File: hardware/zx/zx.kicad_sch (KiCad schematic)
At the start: 51 parts, among them J1 ZX Keyboard, J10 Conn_01x01, J11 Conn_01x01, J12 Conn_01x01, J13 Conn_01x01, J14 Conn_01x01, J15 Conn_01x01, J16 Conn_01x01, J17 Conn_01x01, J18 Conn_01x01, J19 Conn_01x01, J2 GOTEK, J20 Conn_01x01, J21 Conn_01x01, J22 Conn_01x01, J23 Conn_01x01, J24 Conn_01x01, J25 Conn_01x01, J26 Conn_01x01, J27 Conn_01x01, J28 Conn_01x01, J29 Conn_01x01, J3 UART, J30 Conn_01x01, J4 USB_A, J5 USB_A, J6 Keyboard, J7 Mouse, J8 Kempston Mouse, J9 Z80, SW1 RESET, SW2 BOOT0, SW3 BOOT1, U1 CH559L, U2 CH446Q, Y1 12MHz

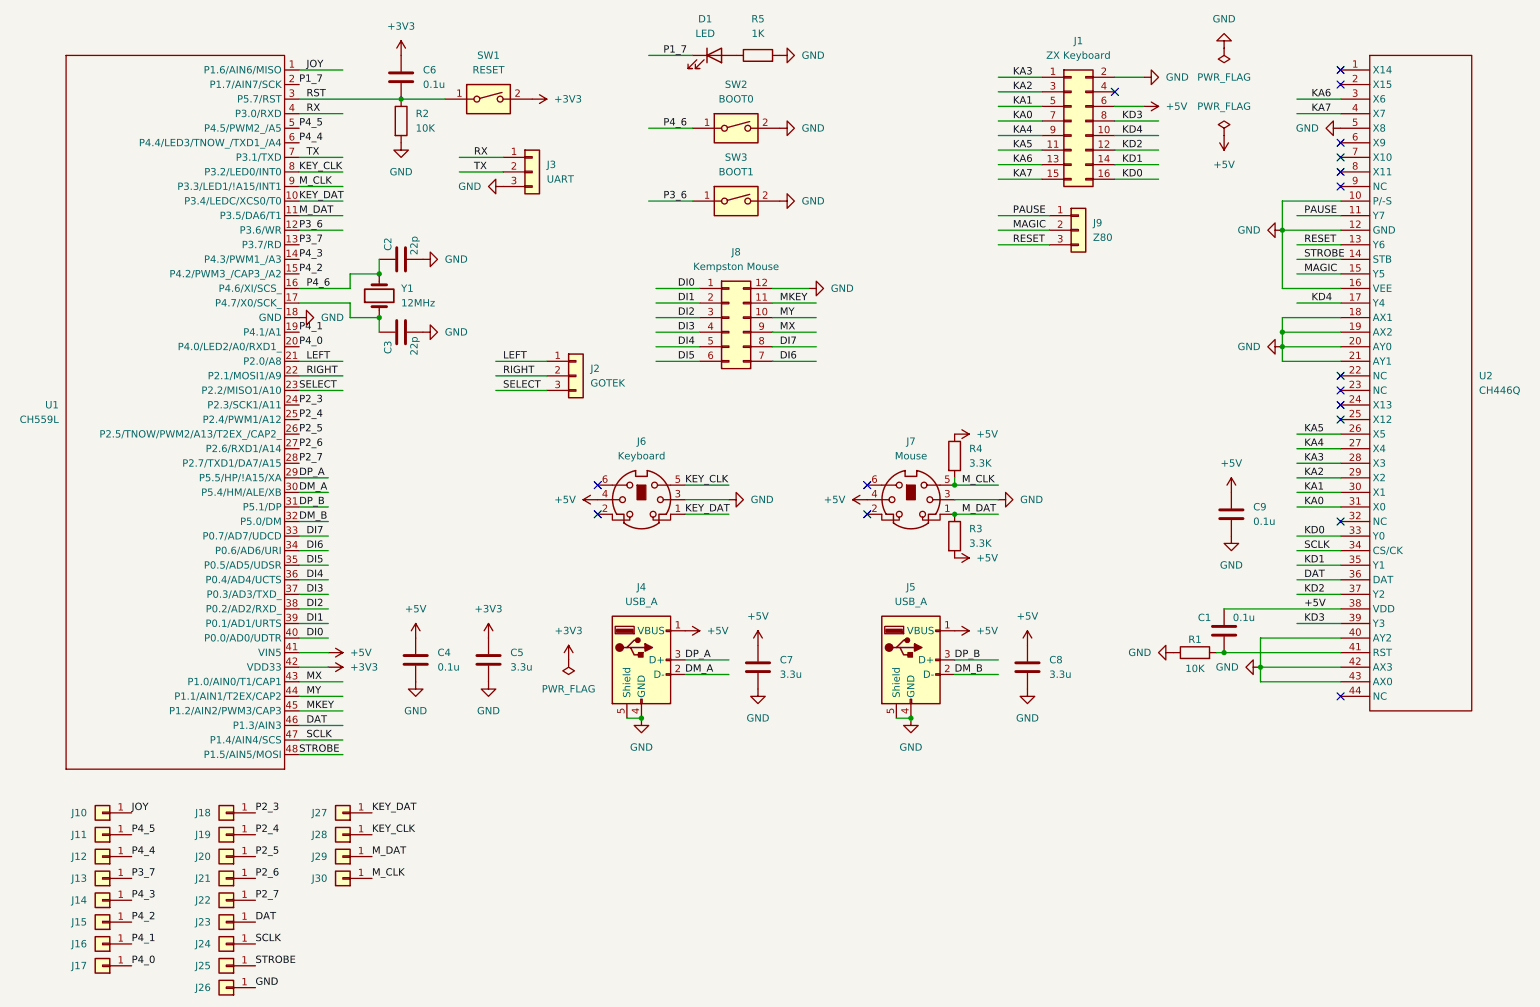
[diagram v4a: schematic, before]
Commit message: Remove BOOT1 switch from schematic. Correct LED polarity.
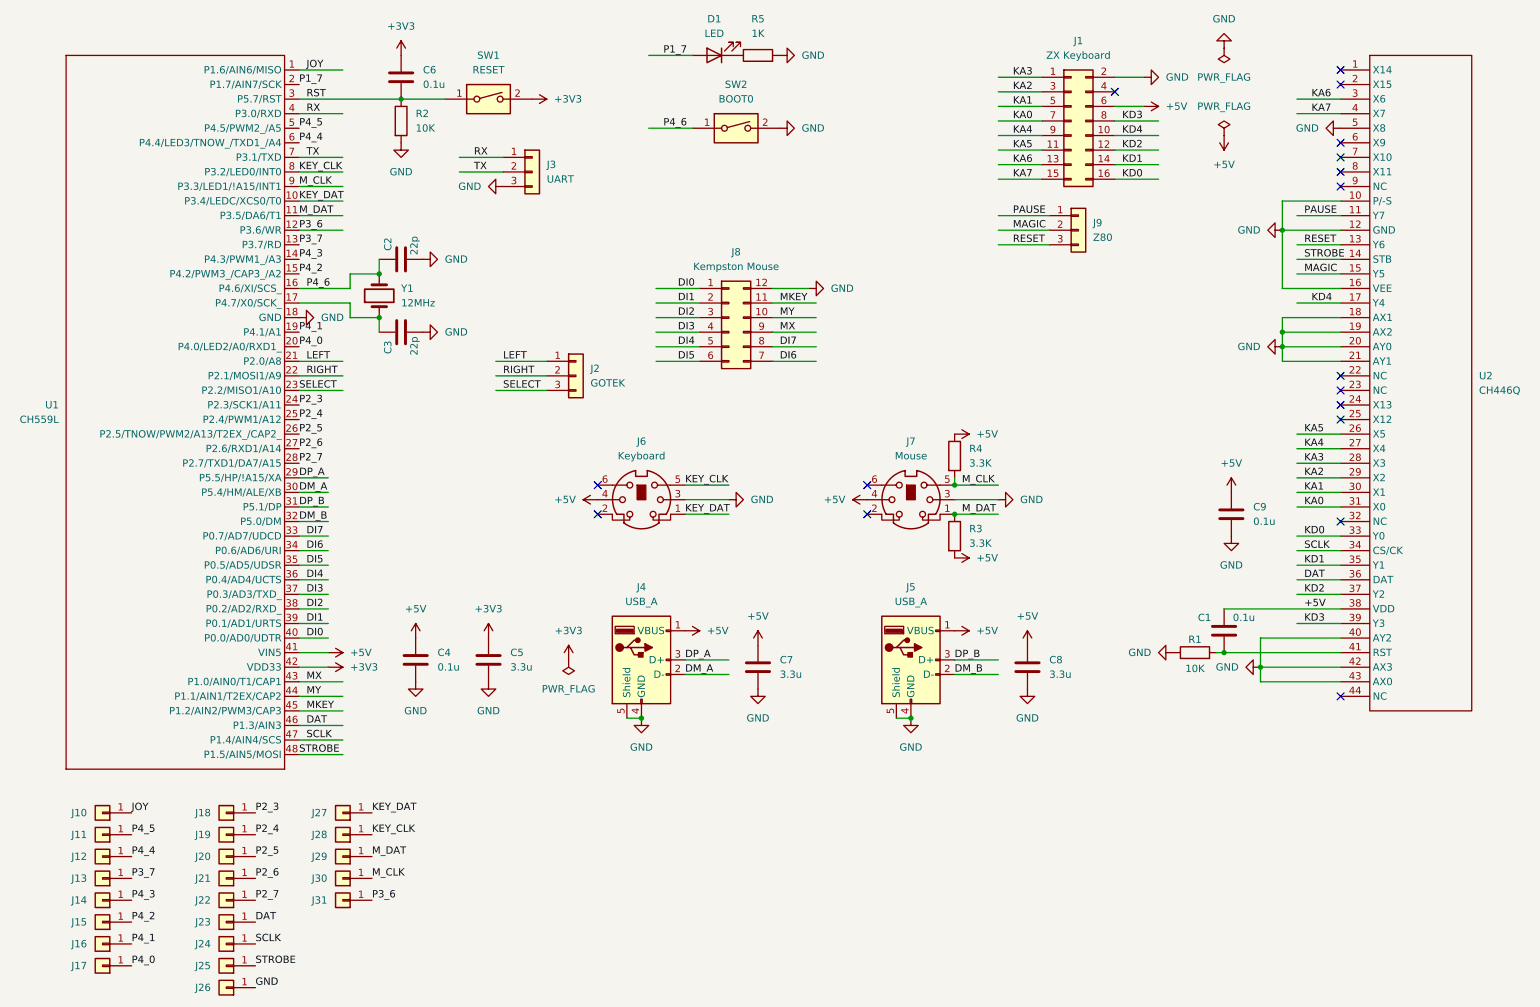
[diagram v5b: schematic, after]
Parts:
- removed SW3: BOOT1, Connector_PinHeader_2.54mm:PinHeader_1x02_P2.54mm_Vertical, symbol Switch:SW_DIP_x01
- added J31: Conn_01x01, THT_Pin:THT_Pin_Vertical, symbol Connector_Generic:Conn_01x01
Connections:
- net P1_7: now also D1.2 (A); no longer D1.1 (K)
- net P3_6: now also J31.1 (Pin_1)
- net at R5.1: now also D1.1 (K); no longer D1.2 (A)
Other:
- moved on the sheet: D1
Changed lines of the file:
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@@
 	(wire
 		(pts
-			(xy 127 46.99) (xy 134.62 46.99)
-		)
-		(stroke
-			(width 0)
-			(type default)
-		)
-	)
-	(wire
-		(pts
 			(xy 148.59 67.31) (xy 156.21 67.31)
 		)
@@
 		)
 	)
-	(label "P3_6"
-		(at 129.54 46.99 0)
-		(fields_autoplaced yes)
-		(effects
-			(font
-				(size 1.27 1.27)
-			)
-			(justify left bottom)
-		)
-	)
 	(label "SELECT"
 		(at 101.6 80.01 0)
@@
 		)
 	)
+	(label "P3_6"
+		(at 78.74 168.91 0)
+		(fields_autoplaced yes)
+		(effects
+			(font
+				(size 1.27 1.27)
+			)
+			(justify left bottom)
+		)
+	)
 	(label "P4_5"
 		(at 66.04 34.29 0)
@@
 	)
 	(symbol
-		(lib_id "Switch:SW_DIP_x01")
-		(at 142.24 46.99 0)
-		(unit 1)
-		(exclude_from_sim no)
-		(in_bom yes)
-		(on_board yes)
-		(dnp no)
-		(fields_autoplaced yes)
-		(property "Reference" "SW3"
-			(at 142.24 39.37 0)
-			(effects
-				(font
-					(size 1.27 1.27)
-				)
-			)
-		)
-		(property "Value" "BOOT1"
-			(at 142.24 41.91 0)
-			(effects
-				(font
-					(size 1.27 1.27)
-				)
-			)
-		)
-		(property "Footprint" "Connector_PinHeader_2.54mm:PinHeader_1x02_P2.54mm_Vertical"
-			(at 142.24 46.99 0)
-			(effects
-				(font
-					(size 1.27 1.27)
-				)
-				(hide yes)
-			)
-		)
-		(property "Datasheet" "~"
-			(at 142.24 46.99 0)
-			(effects
-				(font
-					(size 1.27 1.27)
-				)
-				(hide yes)
-			)
-		)
-		(property "Description" "1x DIP Switch, Single Pole Single Throw (SPST) switch, small symbol"
-			(at 142.24 46.99 0)
-			(effects
-				(font
-					(size 1.27 1.27)
-				)
-				(hide yes)
-			)
-		)
-		(pin "2"
-		)
-		(pin "1"
-		)
-		(instances
-			(project "zx"
-				(path "/e686a5db-35f9-40ca-bbb5-69eb58ec1522"
-					(reference "SW3")
-					(unit 1)
-				)
-			)
-		)
-	)
-	(symbol
 		(lib_id "power:GND")
 		(at 140.97 99.06 90)
@@
 	(symbol
 		(lib_id "Device:LED")
-		(at 138.43 21.59 0)
+		(at 138.43 21.59 180)
 		(unit 1)
 		(exclude_from_sim no)
@@
 		(on_board yes)
 		(dnp no)
-		(fields_autoplaced yes)
 		(property "Reference" "D1"
-			(at 136.8425 15.24 0)
+			(at 138.43 15.24 0)
 			(effects
 				(font
@@
 		)
 		(property "Value" "LED"
-			(at 136.8425 17.78 0)
+			(at 138.43 17.78 0)
 			(effects
 				(font
@@
 	)
 	(symbol
+		(lib_id "Connector_Generic:Conn_01x01")
+		(at 73.66 168.91 180)
+		(unit 1)
+		(exclude_from_sim no)
+		(in_bom yes)
+		(on_board yes)
+		(dnp no)
+		(property "Reference" "J31"
+			(at 69.596 168.91 0)
+			(effects
+				(font
+					(size 1.27 1.27)
+				)
+			)
+		)
+		(property "Value" "Conn_01x01"
+			(at 73.66 165.1 0)
+			(effects
+				(font
+					(size 1.27 1.27)
+				)
+				(hide yes)
+			)
+		)
+		(property "Footprint" "THT_Pin:THT_Pin_Vertical"
+			(at 73.66 168.91 0)
+			(effects
+				(font
+					(size 1.27 1.27)
+				)
+				(hide yes)
+			)
+		)
+		(property "Datasheet" "~"
+			(at 73.66 168.91 0)
+			(effects
+				(font
+					(size 1.27 1.27)
+				)
+				(hide yes)
+			)
+		)
+		(property "Description" "Generic connector, single row, 01x01, script generated (kicad-library-utils/schlib/autogen/connector/)"
+			(at 73.66 168.91 0)
+			(effects
+				(font
+					(size 1.27 1.27)
+				)
+				(hide yes)
+			)
+		)
+		(pin "1"
+		)
+		(instances
+			(project "zx"
+				(path "/e686a5db-35f9-40ca-bbb5-69eb58ec1522"
+					(reference "J31")
+					(unit 1)
+				)
+			)
+		)
+	)
+	(symbol
 		(lib_id "CH559L:CH559L")
 		(at 66.04 30.48 0)
@@
 					(unit 1)
 				)
-			)
-		)
-	)
-	(symbol
-		(lib_id "power:GND")
-		(at 149.86 46.99 90)
-		(unit 1)
-		(exclude_from_sim no)
-		(in_bom yes)
-		(on_board yes)
-		(dnp no)
-		(fields_autoplaced yes)
-		(property "Reference" "#PWR033"
-			(at 156.21 46.99 0)
-			(effects
-				(font
-					(size 1.27 1.27)
-				)
-				(hide yes)
-			)
-		)
-		(property "Value" "GND"
-			(at 153.67 46.9899 90)
-			(effects
-				(font
-					(size 1.27 1.27)
-				)
-				(justify right)
-			)
-		)
-		(property "Footprint" ""
-			(at 149.86 46.99 0)
-			(effects
-				(font
-					(size 1.27 1.27)
-				)
-				(hide yes)
-			)
-		)
-		(property "Datasheet" ""
-			(at 149.86 46.99 0)
-			(effects
-				(font
-					(size 1.27 1.27)
-				)
-				(hide yes)
-			)
-		)
-		(property "Description" "Power symbol creates a global label with name \"GND\" , ground"
-			(at 149.86 46.99 0)
-			(effects
-				(font
-					(size 1.27 1.27)
-				)
-				(hide yes)
-			)
-		)
-		(pin "1"
-		)
-		(instances
-			(project "zx"
-				(path "/e686a5db-35f9-40ca-bbb5-69eb58ec1522"
-					(reference "#PWR033")
-					(unit 1)
-				)

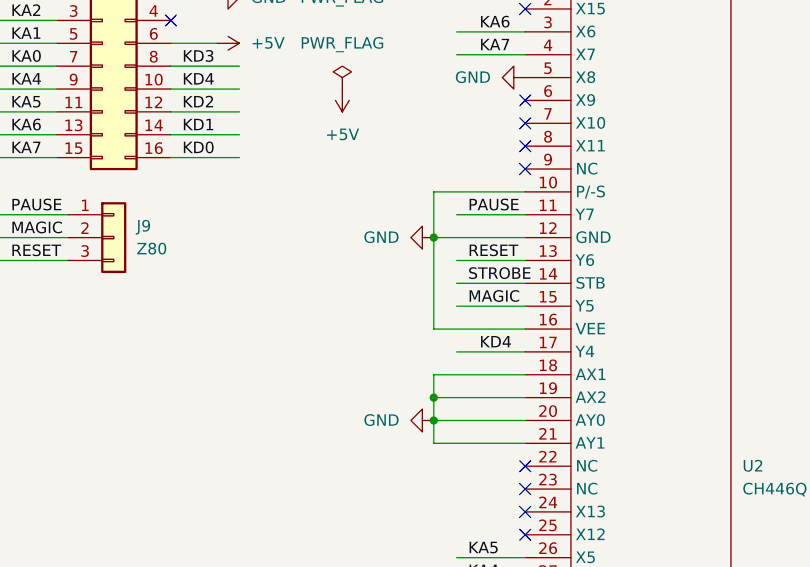
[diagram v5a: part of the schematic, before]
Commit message: Prototype board: Fixed Help screen with Gluk Reset Service after power on. Add 10K pulldown resistor for STB signal, init P1 value before setting port to output.
Fix not required for ZX BUS / CPLD implementation because of rising_edge of STB signal used instead of active high level.
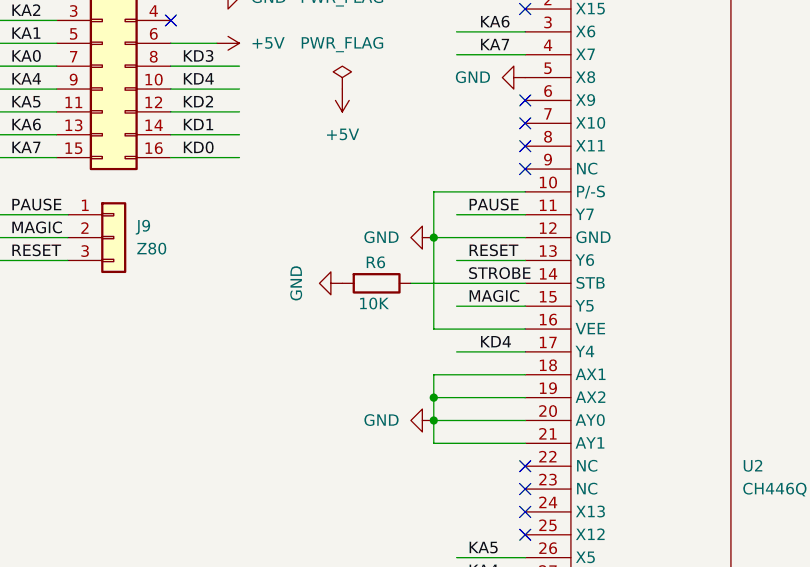
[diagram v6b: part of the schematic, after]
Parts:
- added R6: 10K, Resistor_SMD:R_1206_3216Metric_Pad1.30x1.75mm_HandSolder, symbol Device:R
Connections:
- net GND: now also R6.2
- net STROBE: now also R6.1
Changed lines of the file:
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@@
 	(wire
 		(pts
-			(xy 240.03 57.15) (xy 247.65 57.15)
+			(xy 234.95 57.15) (xy 247.65 57.15)
 		)
 		(stroke
@@
 	)
 	(symbol
+		(lib_id "Device:R")
+		(at 231.14 57.15 270)
+		(unit 1)
+		(exclude_from_sim no)
+		(in_bom yes)
+		(on_board yes)
+		(dnp no)
+		(property "Reference" "R6"
+			(at 229.87 54.864 90)
+			(effects
+				(font
+					(size 1.27 1.27)
+				)
+				(justify left)
+			)
+		)
+		(property "Value" "10K"
+			(at 229.108 59.436 90)
+			(effects
+				(font
+					(size 1.27 1.27)
+				)
+				(justify left)
+			)
+		)
+		(property "Footprint" "Resistor_SMD:R_1206_3216Metric_Pad1.30x1.75mm_HandSolder"
+			(at 231.14 55.372 90)
+			(effects
+				(font
+					(size 1.27 1.27)
+				)
+				(hide yes)
+			)
+		)
+		(property "Datasheet" "~"
+			(at 231.14 57.15 0)
+			(effects
+				(font
+					(size 1.27 1.27)
+				)
+				(hide yes)
+			)
+		)
+		(property "Description" "Resistor"
+			(at 231.14 57.15 0)
+			(effects
+				(font
+					(size 1.27 1.27)
+				)
+				(hide yes)
+			)
+		)
+		(pin "1"
+		)
+		(pin "2"
+		)
+		(instances
+			(project "zx"
+				(path "/e686a5db-35f9-40ca-bbb5-69eb58ec1522"
+					(reference "R6")
+					(unit 1)
+				)
+			)
+		)
+	)
+	(symbol
 		(lib_id "power:GND")
 		(at 140.97 99.06 90)
@@
 					(unit 1)
 				)
+			)
+		)
+	)
+	(symbol
+		(lib_id "power:GND")
+		(at 227.33 57.15 270)
+		(unit 1)
+		(exclude_from_sim no)
+		(in_bom yes)
+		(on_board yes)
+		(dnp no)
+		(fields_autoplaced yes)
+		(property "Reference" "#PWR033"
+			(at 220.98 57.15 0)
+			(effects
+				(font
+					(size 1.27 1.27)
+				)
+				(hide yes)
+			)
+		)
+		(property "Value" "GND"
+			(at 222.25 57.15 0)
+			(effects
+				(font
+					(size 1.27 1.27)
+				)
+			)
+		)
+		(property "Footprint" ""
+			(at 227.33 57.15 0)
+			(effects
+				(font
+					(size 1.27 1.27)
+				)
+				(hide yes)
+			)
+		)
+		(property "Datasheet" ""
+			(at 227.33 57.15 0)
+			(effects
+				(font
+					(size 1.27 1.27)
+				)
+				(hide yes)
+			)
+		)
+		(property "Description" "Power symbol creates a global label with name \"GND\" , ground"
+			(at 227.33 57.15 0)
+			(effects
+				(font
+					(size 1.27 1.27)
+				)
+				(hide yes)
+			)
+		)
+		(pin "1"
+		)
+		(instances
+			(project "zx"
+				(path "/e686a5db-35f9-40ca-bbb5-69eb58ec1522"
+					(reference "#PWR033")
+					(unit 1)
+				)

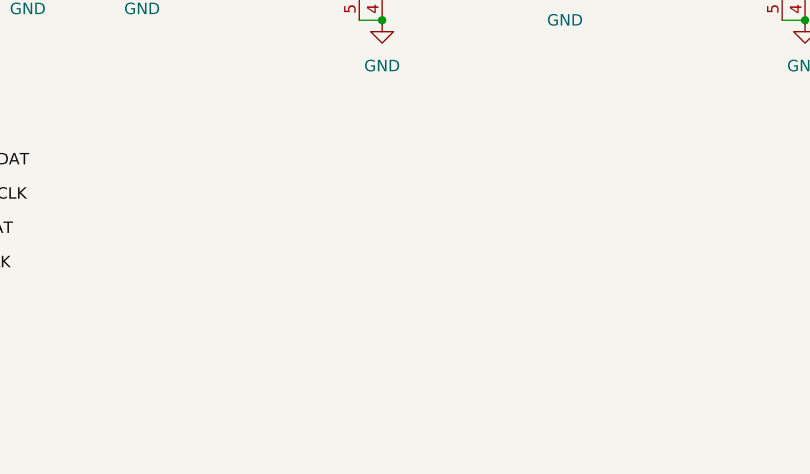
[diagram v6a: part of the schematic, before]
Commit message: Experimental SEGA Mega Drive / Genesis 3-button gamepad support. D-pad, B,A,C buttons, START button translated to Kempston gamepad, button B as primary button.
P2.3 are Sega Mega Drive / Genesis controller SELECT pin (open collector with pullup).
P4 pins 0,1,2,3,4,5 are Sega Mega Drive / Genesis controller data input, open collector with pullups.
Note: P4 supports pure input and push-pull output modes only.
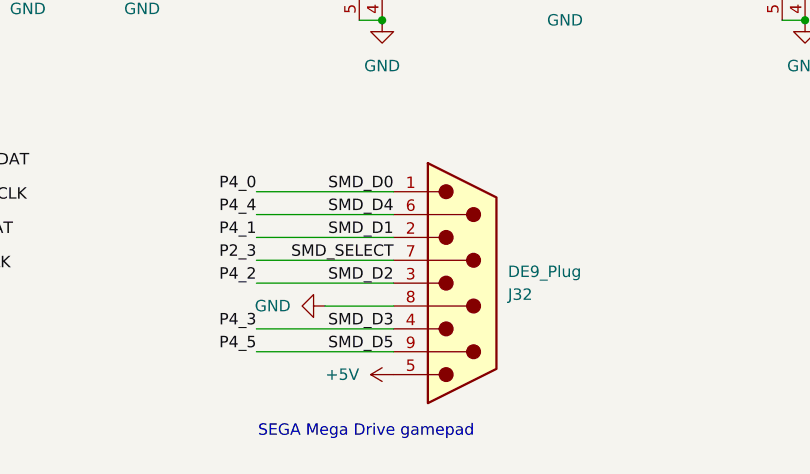
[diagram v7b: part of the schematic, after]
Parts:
- added J32: DE9_Plug, Connector_Dsub:DSUB-9_Male_Horizontal_P2.77x2.84mm_EdgePinOffset7.70mm_Housed_MountingHolesOffset9.12mm, symbol Connector:DE9_Plug
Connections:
- net +5V: now also J32.5
- net GND: now also J32.8
- net P2_3: now also J32.7
- net P4_0: now also J32.1
- net P4_1: now also J32.2
- net P4_2: now also J32.3
- net P4_3: now also J32.4
- net P4_4: now also J32.6
- net P4_5: now also J32.9
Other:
- note added: "SEGA Mega Drive gamepad"
